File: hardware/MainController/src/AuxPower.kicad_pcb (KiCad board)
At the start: 2 copper layers, 90 x 90 mm, 123 parts, among them J1 MC 1,5/2, J10 MC 1,5/4, J11 S3B-XH-A, J12 S3B-XH-A, J13 S3B-XH-A, J14 S3B-XH-A, J15 S3B-XH-A, J16 B3B-XH-A, J17 B4B-XH-A, J2 MC 1,5/2, J3 MC 1,5/2, J4 MC 1,5/2, J5 MC 1,5/2, J6 MC 1,5/4, J7 MC 1,5/4, J8 MC 1,5/4, J9 MC 1,5/4, Q1 BC846B,235, Q10 AO4421, Q2 BC846B,235, Q3 BC846B,235, Q4 BC846B,235, Q5 BC846B,235, Q6 AO4421, Q7 AO4421, Q8 AO4421, Q9 AO4421, U1 ZXCT1009, U2 ZXCT1009, U3 ZXCT1009, U5 ZXCT1009, U6 PIC18F26K83, U7 PI4IOE5V6416, U8 MCP9701

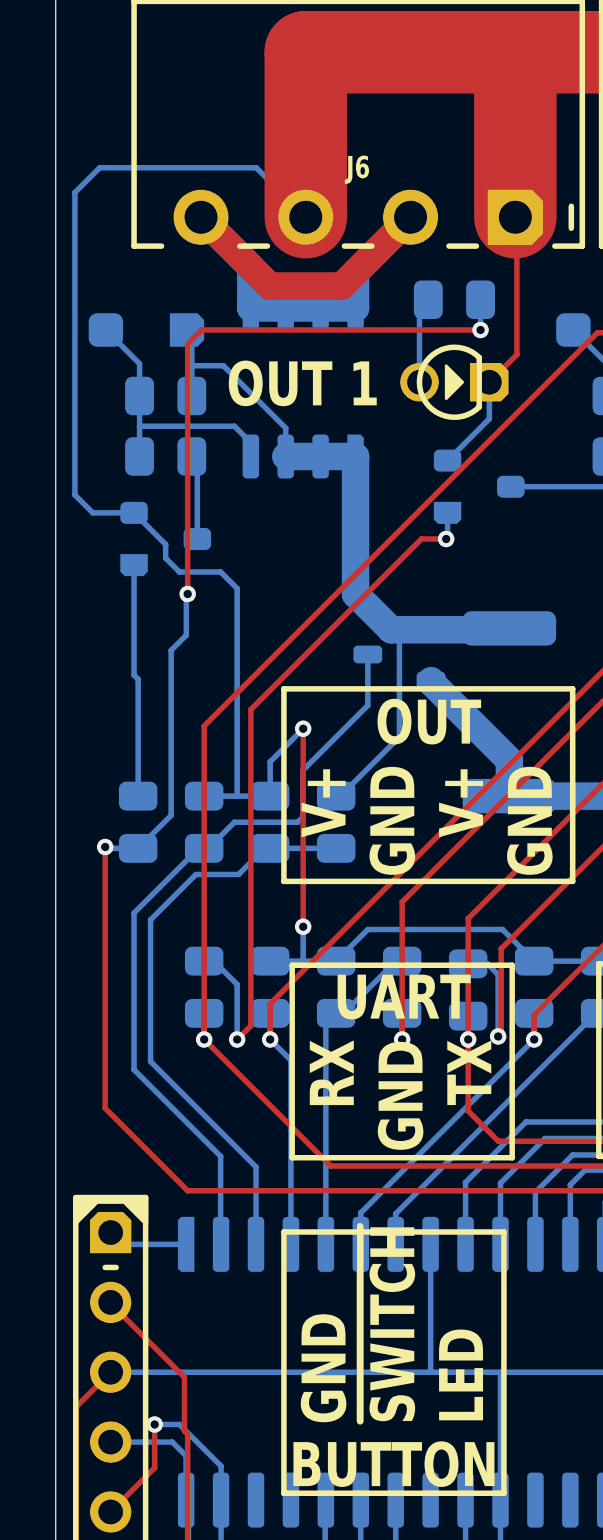
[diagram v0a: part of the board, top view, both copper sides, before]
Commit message: Moved GND line to look nicer
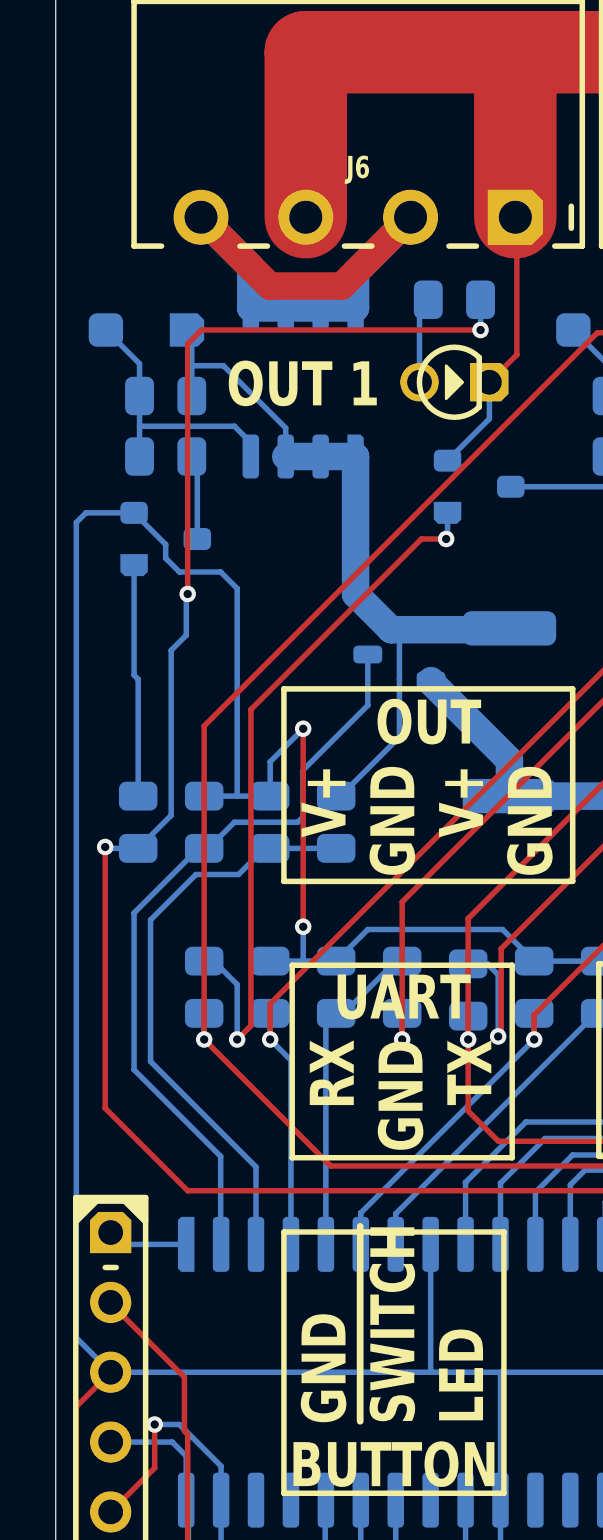
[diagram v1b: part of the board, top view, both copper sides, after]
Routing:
- net GND: track 698.2 -> 708.9 mm
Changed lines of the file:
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@@
-	)
-	(segment
-		(start 17.85 33.75)
-		(end 16.35 33.75)
-		(width 0.2)
-		(layer "B.Cu")
-		(net 1)
 	)
 	(segment
@@
 	)
 	(segment
-		(start 16.6 21.2)
-		(end 22.295 21.2)
-		(width 0.2)
-		(layer "B.Cu")
-		(net 1)
-	)
-	(segment
-		(start 16.35 33.75)
-		(end 15.7 33.1)
-		(width 0.2)
-		(layer "B.Cu")
-		(net 1)
-	)
-	(segment
 		(start 42 50.05)
 		(end 40.85 48.9)
@@
 	)
 	(segment
-		(start 22.295 21.2)
-		(end 24.095 23)
-		(width 0.2)
-		(layer "B.Cu")
-		(net 1)
-	)
-	(segment
 		(start 57.375 64.35)
 		(end 55 64.35)
@@
 	)
 	(segment
-		(start 15.7 22.1)
-		(end 16.6 21.2)
+		(start 17.85 33.75)
+		(end 16.1 33.75)
 		(width 0.2)
 		(layer "B.Cu")
@@
 	)
 	(segment
+		(start 15.75 63.75)
+		(end 17 65)
+		(width 0.2)
+		(layer "B.Cu")
+		(net 1)
+	)
+	(segment
 		(start 38.5 65)
 		(end 38.5 69.9)
@@
 	)
 	(segment
-		(start 15.7 33.1)
-		(end 15.7 22.1)
-		(width 0.2)
-		(layer "B.Cu")
-		(net 1)
-	)
-	(segment
 		(start 50.8 76.6)
 		(end 49.9 75.7)
@@
 	)
 	(segment
+		(start 16.1 33.75)
+		(end 15.75 34.1)
+		(width 0.2)
+		(layer "B.Cu")
+		(net 1)
+	)
+	(segment
 		(start 22.8 44.05)
 		(end 22.8 42.80001)
 		(width 0.2)
 		(layer "B.Cu")
+		(net 1)
+	)
+	(segment
+		(start 15.75 34.1)
+		(end 15.75 63.75)
+		(width 0.2)
+		(layer "B.Cu")

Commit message: Increasing resistors to account for 55V supply
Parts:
- R53, R54, R55, R56: value 15K -> 18K
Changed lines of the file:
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@@
 			)
 		)
-		(property "Value" "15K"
+		(property "Value" "18K"
 			(at 2.8 0 0)
 			(layer "B.SilkS")
@@
 			)
 		)
-		(property "Value" "15K"
+		(property "Value" "18K"
 			(at 2.8 0 0)
 			(layer "B.SilkS")
@@
 			)
 		)
-		(property "Value" "15K"
+		(property "Value" "18K"
 			(at 2.8 0 0)
 			(layer "B.SilkS")
@@
 			)
 		)
-		(property "Value" "15K"
+		(property "Value" "18K"
 			(at 2.8 0 0)
 			(layer "B.SilkS")
